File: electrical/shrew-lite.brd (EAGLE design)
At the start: 15.5 x 24 mm, 47 parts, among them IC1 Vreg +3V3, U1 ESP32-PICO-D4, U2 SX1280IMLTRT, U3 DRV8231DSGR, U4 DRV8231DSGR, X1 PIN-1X-BIG, X2 PIN-1X-BIG, X3 PIN-1X-BIG, X4 PIN-1X-BIG, X5 PIN-1X-MED, X6 PIN-1X-MED, X7 PIN-1X-MED, X8 PIN-1X-MED, Y1 52MHz TCXO

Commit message: sorted component ref des
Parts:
- removed EDGE1: (no value), shrew-common:1X05
- removed FL1: 2450FM07D0034T, shrew-core:FIL_2450FM07D0034T
- added JP2: (no value), shrew-common:1X07-2MM-TH-TINY
- added Y2: 52MHz TCXO, shrew-common:OSC_TG2016SMN_50.0000M-ECGNNMB
- C1: value 1n -> 10u; device shrew-common:0402-REV -> shrew-common:0805
- C10: value 100n -> 470n
- C11: value 10u -> DNP; device shrew-common:0805 -> shrew-common:0402-CAP
- C12: value DNP -> 470n; device shrew-common:0402-CAP -> shrew-common:0402-REV
- C13: value 470n -> 10n
- C14: value 100n -> 10n; device shrew-common:0402-CAP -> shrew-common:0402-REV
- C15: value 100n -> 1n; device shrew-common:0402-CAP -> shrew-common:0402-REV
- C16, C18: value 10u -> 100n; device shrew-common:0805 -> shrew-common:0402-REV
- C17: value 470n -> 100n
- C19: value 10u -> 470n; device shrew-common:0805 -> shrew-common:0402-REV
- C2: value 470n -> 10u; device shrew-common:0402-REV -> shrew-common:0805
- C20, C21: value 10u -> 100n; device shrew-common:0805 -> shrew-common:0402-CAP
- C3, C4: value 10n -> 10u; device shrew-common:0402-REV -> shrew-common:0805
- C5, C9: value 100n -> 10u; device shrew-common:0402-REV -> shrew-common:0805
- JP1: device shrew-common:1X07-2MM-TH-TINY -> shrew-common:1X05
- R2: value 10K -> 68K; device shrew-common:0402-REV -> shrew-common:0402-RES
- R4: value 68K -> 10K; device shrew-common:0402-RES -> shrew-common:0402-REV
- X1, X2, X3, X4: value PIN-1X-BIG -> PIN-1X-MED; device shrew-core:PAD-1X-BIG -> shrew-core:PAD-1X-MED
- X5, X6, X7, X8: value PIN-1X-MED -> PIN-1X-BIG; device shrew-core:PAD-1X-MED -> shrew-core:PAD-1X-BIG
- Y1: value 52MHz TCXO -> 2450FM07D0034T; device shrew-common:OSC_TG2016SMN_50.0000M-ECGNNMB -> shrew-core:FIL_2450FM07D0034T
- moved C14 18.3 mm to (6.00, 21.6), turned to 270 degrees
- moved C15 16.9 mm to (5.30, 18.8), turned to 0 degrees
- moved C4 16.4 mm to (9.70, 6.00), turned to 90 degrees
- moved C3 15.7 mm to (8.05, 6.00), turned to 90 degrees
- moved C5 14.4 mm to (2.90, 8.80), flipped to the bottom, turned to 180 degrees
- moved C1 13.3 mm to (13.9, 8.60), flipped to the bottom, turned to 180 degrees
- moved C18 13.0 mm to (14.6, 17.2)
- moved C2 11.2 mm to (6.40, 6.00), turned to 90 degrees
- moved C13 10.1 mm to (4.70, 21.6), flipped to the top, turned to 270 degrees
- moved C10 9.63 mm to (14.8, 21.0)
- moved C19 9.49 mm to (13.5, 14.7), turned to 180 degrees
- moved C16 9.07 mm to (5.30, 15.0), turned to 180 degrees
- moved C6 8.08 mm to (5.20, 21.7), flipped to the bottom, turned to 90 degrees
- moved JP1 7.23 mm to (1.50, 11.8), turned to 90 degrees
- moved Y1 6.82 mm to (9.05, 22.6)
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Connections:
- net +24V: now also C2.1, C3.1, C4.1, C5.1, R2.2, X1.1, X2.1; no longer C16.1, C18.1, C19.1, C20.1, R4.2, X5.1, X7.1
- net 3.3V: now also C1.1, C16.2, C17.2, C18.2, C6.1, C7.1, JP2.2, Y2.4; no longer C10.1, C11.1, C21.1, C5.2, C6.2, C7.2, JP1.2, Y1.4
- net AUX1: now also JP1.1; no longer EDGE1.1
- net AUX2: now also JP1.2; no longer EDGE1.2
- net BATT-ADC: now also C12.1, R4.2; no longer C17.1, R2.2
- net ESP-BOOT: now also C11.2; no longer C12.2
- net ESP-EN: now also C10.2; no longer C13.2
- net GND: now also C1.2, C10.1, C11.1, C12.2, C14.1, C16.1, C17.1, C18.1, C19.1, C2.2, C3.2, C4.2, C5.2, C6.2, C7.2, JP1.5, JP2.1, R4.1, X3.1, X4.1, Y1.4, Y2.2; no longer C10.2, C11.2, C12.1, C16.2, C17.2, C18.2, C19.2, C2.1, C20.2, C21.2, C3.1, C4.1, C5.1, C6.1, C7.1, EDGE1.5, FL1.2, FL1.4, JP1.1, R2.1, X6.1, X8.1
- net MOTOR1: now also C21.2, X8.1; no longer C15.2, X3.1
- net MOTOR2: now also C21.1, X6.1; no longer C15.1, X4.1
- net MOTOR3: now also C20.2, X7.1; no longer C14.2, X1.1
- net MOTOR4: now also C20.1, X5.1; no longer C14.1, X2.1
- net N$11: now also C14.2; no longer C3.2
- net N$2: now also C15.1, Y2.3; no longer C1.1, Y1.3
- net N$3: now also C15.2; no longer C1.2
- net N$4: now also JP2.3, R2.1; no longer JP1.3, R4.1
- net N$6: now also Y1.1; no longer FL1.1
- net N$7: now also Y1.3; no longer FL1.3
- net RADIO-VDD: now also C13.2, C19.2; no longer C2.2, C4.2
- net SIG1: now also JP2.4; no longer JP1.4
- net SIG2: now also JP2.5; no longer JP1.5
- net SIG3: now also JP2.6; no longer JP1.6
- net SIG4: now also JP2.7; no longer JP1.7
- net U0RXD: now also JP1.3; no longer EDGE1.3
- net U0TXD: now also JP1.4; no longer EDGE1.4

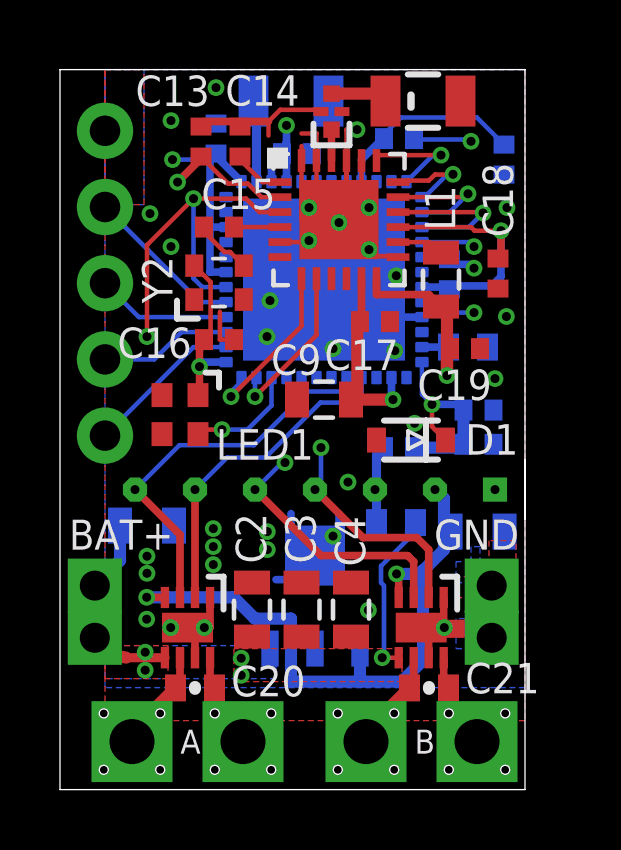
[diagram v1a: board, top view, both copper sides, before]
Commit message: shrew pro prototype sent off to manufacturing
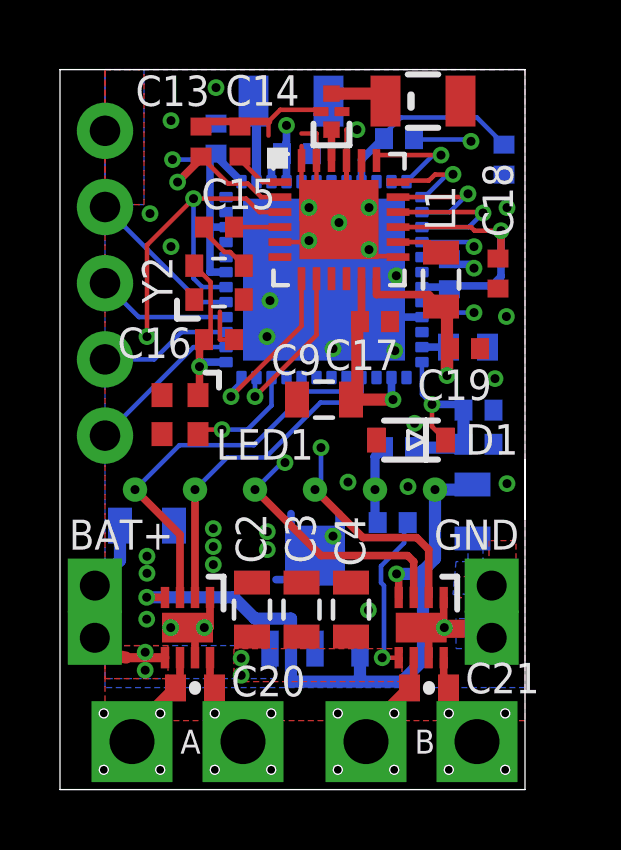
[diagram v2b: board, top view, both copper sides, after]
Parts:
- removed JP2: (no value), shrew-common:1X07-2MM-TH-TINY
- R2: device shrew-common:0402-RES -> shrew-common:0402-REV
- moved C1 0.69 mm to (13.8, 9.27), turned to 270 degrees
- moved R2 0.11 mm to (11.1, 8.90)
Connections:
- net 3.3V: no longer JP2.2
- net GND: no longer JP2.1
- net N$4: no longer JP2.3
- net SIG1: no longer JP2.4
- net SIG2: no longer JP2.5
- net SIG3: no longer JP2.6
- net SIG4: no longer JP2.7
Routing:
- net 3.3V: track 56.1 -> 56.9 mm, vias 8 -> 9
- net N$4: track 2.65 -> 2.67 mm, vias 0 -> 1
- net SIG3: vias 0 -> 1
- net SIG2: vias 2 -> 3
- net SIG4: vias 0 -> 1
- net SIG1: vias 2 -> 3
- net GND: vias 34 -> 36

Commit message: shrew-lite new buck vreg
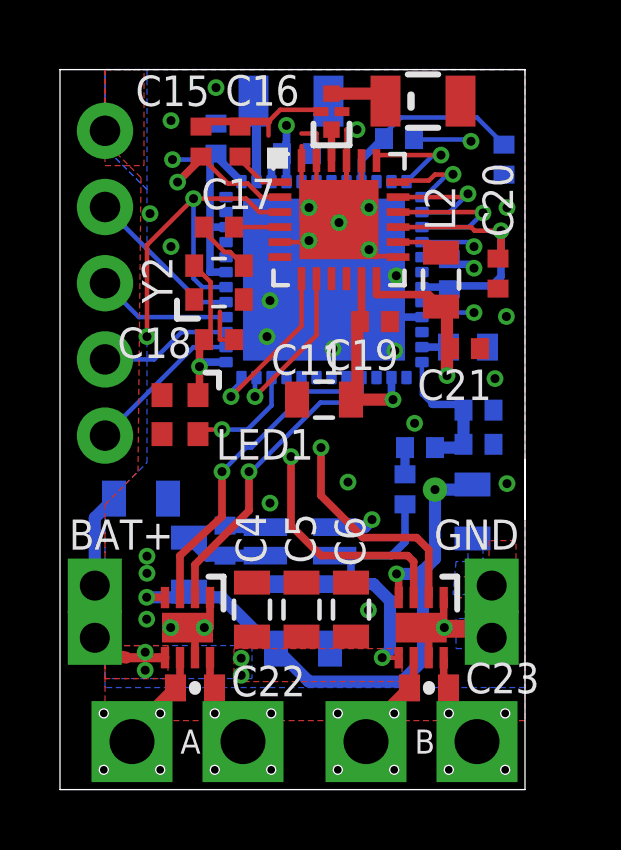
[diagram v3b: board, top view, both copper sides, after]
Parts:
- removed D1: 3V6, shrew-common:SOD-323
- added C22, C23: 100n, shrew-common:0402-CAP
- added L2: 15u, shrew-common:0805
- C1, C9: value 10u -> 100n; device shrew-common:0805 -> shrew-common:0402-REV
- C10, C19: value 470n -> 100n
- C11: value DNP -> 10u; device shrew-common:0402-CAP -> shrew-common:0805
- C13: value 10n -> DNP; device shrew-common:0402-REV -> shrew-common:0402-CAP
- C14: value 10n -> 470n
- C15: value 1n -> 10n
- C16: value 100n -> 10n
- C17: value 100n -> 1n
- C2, C3: value 10u -> 22u
- C20: device shrew-common:0402-CAP -> shrew-common:0402-REV
- C21: value 100n -> 470n; device shrew-common:0402-CAP -> shrew-common:0402-REV
- C6, C7: value 100n -> 10u; device shrew-common:0402-REV -> shrew-common:0805
- IC1: value Vreg +3V3 -> AP63203WU; device shrew-common:SOT89 -> shrew-core:SOT95P280X110-6N
- L1: value 15u -> 10u
- moved C20 17.1 mm to (14.6, 17.2), turned to 90 degrees
- moved C6 16.3 mm to (9.70, 6.00), flipped to the top
- moved L1 12.7 mm to (4.30, 7.50), flipped to the bottom, turned to 270 degrees
- moved C7 12.6 mm to (2.70, 9.70)
- moved C14 12.0 mm to (13.9, 12.7), flipped to the bottom, turned to 180 degrees
- moved C21 11.4 mm to (13.5, 14.7)
- moved C13 11.2 mm to (13.6, 14.8), flipped to the bottom, turned to 0 degrees
- moved C18 9.56 mm to (5.30, 15.0), turned to 180 degrees
- moved C8 9.00 mm to (5.20, 21.7)
- moved C12 8.39 mm to (14.8, 21.0), turned to 90 degrees
- moved C1 8.31 mm to (5.50, 8.30)
- moved C9 8.25 mm to (7.90, 21.2), flipped to the bottom
- moved C2 8.04 mm to (13.8, 9.27), flipped to the bottom, turned to 270 degrees
- moved C16 6.64 mm to (6.00, 21.6), turned to 270 degrees
- moved C17 6.08 mm to (5.30, 18.8), turned to 0 degrees
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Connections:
- new net N$10: C1.2, IC1.5, L1.1
- new net N$12: C1.1, IC1.6
- net +24V: now also C6.1, C7.1, IC1.2; no longer C2.1, C3.1
- net 3.3V: now also C10.1, C11.1, C19.2, C2.1, C20.2, C3.1, L1.2; no longer C1.1, C16.2, C17.2, C6.1, C7.1
- net BATT-ADC: now also C14.1; no longer C12.1, D1.1
- net ESP-BOOT: now also C13.2; no longer C11.2
- net ESP-EN: now also C12.2; no longer C10.2
- net GND: now also C10.2, C11.2, C12.1, C14.2, C15.1, C20.1, C21.1; no longer C1.2, C10.1, C11.1, C12.2, C14.1, C17.1, D1.2, IC1.2
- net MOTOR1: now also C23.2; no longer C21.2
- net MOTOR2: now also C23.1; no longer C21.1
- net MOTOR3: now also C22.2; no longer C20.2
- net MOTOR4: now also C22.1; no longer C20.1
- net N$11: now also C16.2; no longer C14.2
- net N$2: now also C17.1; no longer C15.1
- net N$3: now also C17.2; no longer C15.2
- net N$9: now also L2.2; no longer L1.2
- net RADIO-VDD: now also C15.2, C21.2, L2.1; no longer C13.2, C19.2, L1.1
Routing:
- net GND: track 50.2 -> 44.6 mm, vias 36 -> 30
- net +24V: track 12.1 -> 16.8 mm
- net N$10: track 0.00 -> 2.79 mm
- net SIG4: track 13.0 -> 10.5 mm
- net BATT-ADC: track 6.98 -> 4.90 mm, vias 1 -> 0
- net N$4: track 2.67 -> 0.89 mm, vias 1 -> 0
- net N$12: track 0.00 -> 1.37 mm
- net SIG2: track 22.0 -> 20.9 mm, vias 3 -> 2
- net 3.3V: track 56.9 -> 56.1 mm, vias 9 -> 10
- net SIG3: track 11.0 -> 10.3 mm
- net SIG1: track 17.2 -> 17.0 mm, vias 3 -> 2

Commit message: shrew-lite buck vreg wip, shorter
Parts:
- added C24, C25, C26: 10u, shrew-common:0402-REV
- added JP2: (no value), shrew-common:1X01-1.0MM-TP
- C11: device shrew-common:0805 -> shrew-common:0402-REV
- C2, C3: value 22u -> 10u; device shrew-common:0805 -> shrew-common:0402-REV
- moved C3 7.42 mm to (13.4, 9.90), flipped to the top, turned to 0 degrees
- moved R2 1.74 mm to (10.0, 10.9), turned to 0 degrees
- moved C7 1.24 mm to (2.40, 8.50), flipped to the top, turned to 0 degrees
- moved ANT1 1.00 mm to (7.70, 21.9)
- moved ANT2 1.00 mm to (12.1, 21.9)
- moved C10 1.00 mm to (13.0, 16.2)
- moved C12 1.00 mm to (14.8, 20.0)
- moved C13 1.00 mm to (13.6, 13.8)
- moved C15 1.00 mm to (4.70, 20.6)
- moved C16 1.00 mm to (6.00, 20.6)
- moved C17 1.00 mm to (5.30, 17.8)
- moved C18 1.00 mm to (5.30, 14.0)
- moved C19 1.00 mm to (10.5, 14.6)
- moved C20 1.00 mm to (14.6, 16.2)
- moved C21 1.00 mm to (13.5, 13.7)
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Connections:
- net 3.3V: now also C24.1, C25.1, C26.1, JP2.1
- net GND: now also C24.2, C25.2, C26.2
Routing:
- net 3.3V: track 56.1 -> 62.4 mm, vias 10 -> 9
- net RADIO-RST: track 12.2 -> 6.93 mm, vias 2 -> 1
- net SIG2: track 20.9 -> 19.1 mm
- net SIG1: track 17.0 -> 15.9 mm
- net SIG4: track 10.5 -> 9.44 mm
- net SIG3: track 10.3 -> 9.26 mm
- net GND: track 44.6 -> 43.9 mm, vias 30 -> 26
- net +24V: track 16.8 -> 17.5 mm
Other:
- board size 15.5 x 24 mm -> 15.5 x 23 mm
- board text added: "#1"
- board text added: "#19"
- board text added: "#22"
- board text added: "#3"
- board text removed: "1"
- board text removed: "19"
- board text removed: "22"
- board text removed: "3"
- board text removed: "BAT+"

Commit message: shrew-lite another prototype order
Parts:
- C10, C8, C9: value 100n -> 10u; device shrew-common:0402-REV -> shrew-common:0805
- C11: value 10u -> 100n
- C12, C21: value 470n -> 100n
- C13: value DNP -> 100n; device shrew-common:0402-CAP -> shrew-common:0402-REV
- C14: value 470n -> 10u
- C15: value 10n -> 470n
- C16: value 10n -> DNP; device shrew-common:0402-REV -> shrew-common:0402-CAP
- C17: value 1n -> 470n
- C18, C19: value 100n -> 10n
- C20: value 100n -> 1n
- C22, C23: device shrew-common:0402-CAP -> shrew-common:0402-REV
- C24: value 10u -> 470n
- C25, C26: value 10u -> 100n; device shrew-common:0402-REV -> shrew-common:0402-CAP
- C4, C5, C6: device shrew-common:0805 -> shrew-common:0402-REV
- JP1: device shrew-common:1X05 -> shrew-common:1X01-1.0MM-TP
- JP2: device shrew-common:1X01-1.0MM-TP -> shrew-common:1X05
- L1: value 10u -> 10uH
- moved C8 15.0 mm to (8.05, 6.00), flipped to the top
- moved C9 14.3 mm to (9.70, 6.00), flipped to the top, turned to 90 degrees
- moved C10 13.1 mm to (2.40, 8.50), flipped to the top, turned to 0 degrees
- moved C23 13.0 mm to (14.6, 16.2), turned to 90 degrees
- moved C22 12.7 mm to (10.5, 14.6)
- moved JP1 11.1 mm to (12.5, 9.00), flipped to the bottom, turned to 0 degrees
- moved JP2 11.1 mm to (1.50, 10.8), flipped to the top, turned to 90 degrees
- moved C17 10.4 mm to (13.9, 12.1), flipped to the bottom, turned to 180 degrees
- moved C16 10.2 mm to (13.6, 13.8), flipped to the bottom, turned to 0 degrees
- moved C15 10.1 mm to (14.8, 20.0), flipped to the bottom, turned to 90 degrees
- moved C25 9.61 mm to (4.50, 3.39)
- moved C20 9.43 mm to (5.30, 17.8), turned to 0 degrees
- moved C11 9.08 mm to (5.20, 20.7), flipped to the bottom, turned to 90 degrees
- moved C4 8.66 mm to (13.4, 11.1), turned to 0 degrees
- moved C21 8.21 mm to (5.30, 14.0)
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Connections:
- net +24V: now also C10.1, C8.1, C9.1; no longer C4.1, C5.1, C6.1
- net 3.3V: now also C12.1, C13.1, C14.1, C21.2, C22.2, C23.2, C4.1, C5.1, C6.1, JP1.1; no longer C10.1, C18.2, C19.2, C20.2, C24.1, C25.1, C26.1, C8.1, C9.1, JP2.1
- net AUX1: now also JP2.1; no longer JP1.1
- net AUX2: now also JP2.2; no longer JP1.2
- net BATT-ADC: now also C17.1; no longer C14.1
- net ESP-BOOT: now also C16.2; no longer C13.2
- net ESP-EN: now also C15.2; no longer C12.2
- net GND: now also C12.2, C13.2, C17.2, C22.1, C23.1, C24.1, JP2.5; no longer C12.1, C13.1, C20.1, C24.2, C25.2, C26.2, JP1.5
- net MOTOR1: now also C26.2; no longer C23.2
- net MOTOR2: now also C26.1; no longer C23.1
- net MOTOR3: now also C25.2; no longer C22.2
- net MOTOR4: now also C25.1; no longer C22.1
- net N$11: now also C19.2; no longer C16.2
- net N$2: now also C20.1; no longer C17.1
- net N$3: now also C20.2; no longer C17.2
- net RADIO-VDD: now also C18.2, C24.2; no longer C15.2, C21.2
- net U0RXD: now also JP2.3; no longer JP1.3
- net U0TXD: now also JP2.4; no longer JP1.4
